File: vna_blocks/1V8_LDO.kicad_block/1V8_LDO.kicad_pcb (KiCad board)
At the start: 4 copper layers, 8 parts, among them U39 LT3041ADE-PBF

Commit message: hmc7044 design block
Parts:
- removed C347, C351, C353: 10u, Capacitor_SMD:C_0402_1005Metric
- removed C349: 4.7u, Capacitor_SMD:C_0603_1608Metric
- removed R190: 18k, Resistor_SMD:R_0402_1005Metric
- removed R193: 43k, Resistor_SMD:R_0402_1005Metric
- removed R194: 10k, Resistor_SMD:R_0402_1005Metric
- removed U39: LT3041ADE-PBF, VNA_fp:05-08-1708_ADI-L
- added C346: 10u, Capacitor_SMD:C_0402_1005Metric, B.Cu at (238.8, 96.0)
- added C348: 4.7u, Capacitor_SMD:C_0603_1608Metric, B.Cu at (241.2, 103.6)
- added C350: 10u, Capacitor_SMD:C_0402_1005Metric, B.Cu at (238.4, 101.4)
- added C352: 10u, Capacitor_SMD:C_0402_1005Metric, B.Cu at (238.4, 102.6)
- added R189: 18k, Resistor_SMD:R_0402_1005Metric, B.Cu at (241.0, 101.4)
- added R191: 43k, Resistor_SMD:R_0402_1005Metric, B.Cu at (242.8, 102.0)
- added R192: 10k, Resistor_SMD:R_0402_1005Metric, B.Cu at (244.4, 101.4)
- added U38: LT3041ADE-PBF, VNA_fp:05-08-1708_ADI-L, B.Cu at (240.4, 98.8)

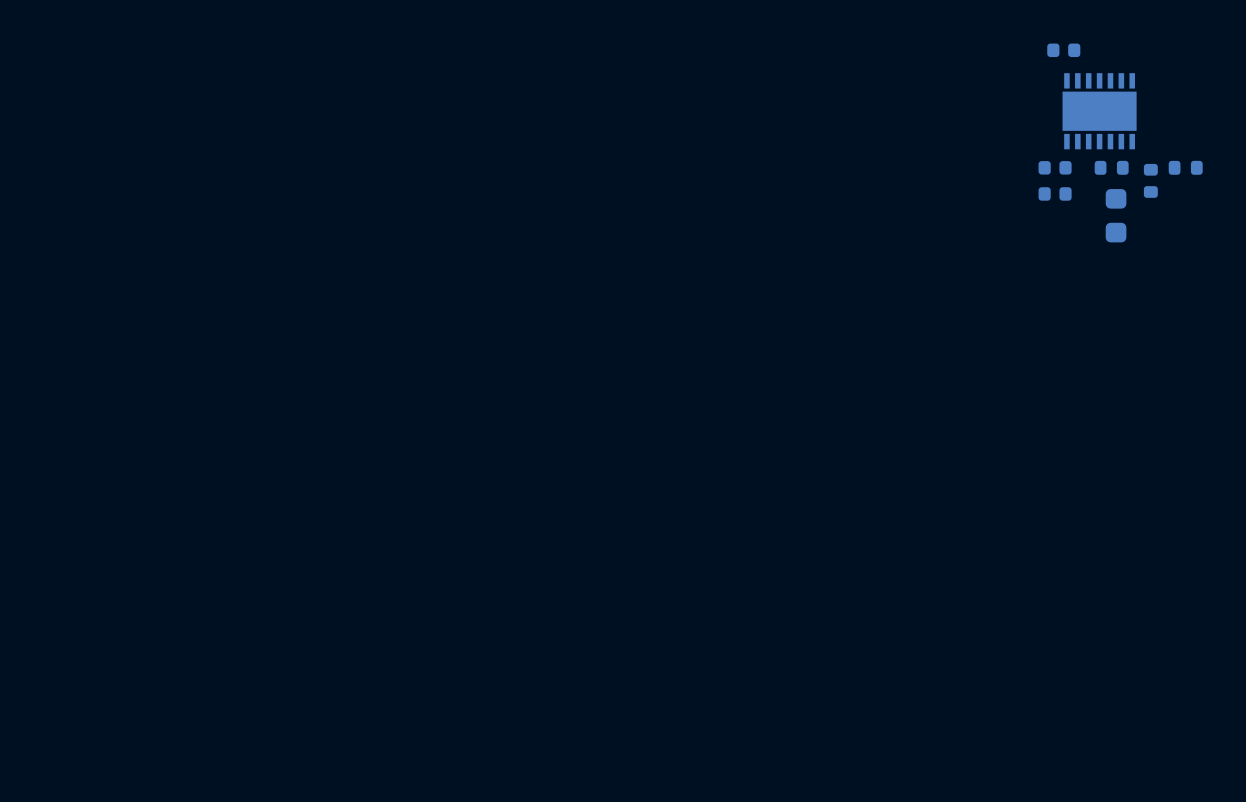
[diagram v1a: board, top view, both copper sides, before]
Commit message: fixed IC courtyard issues
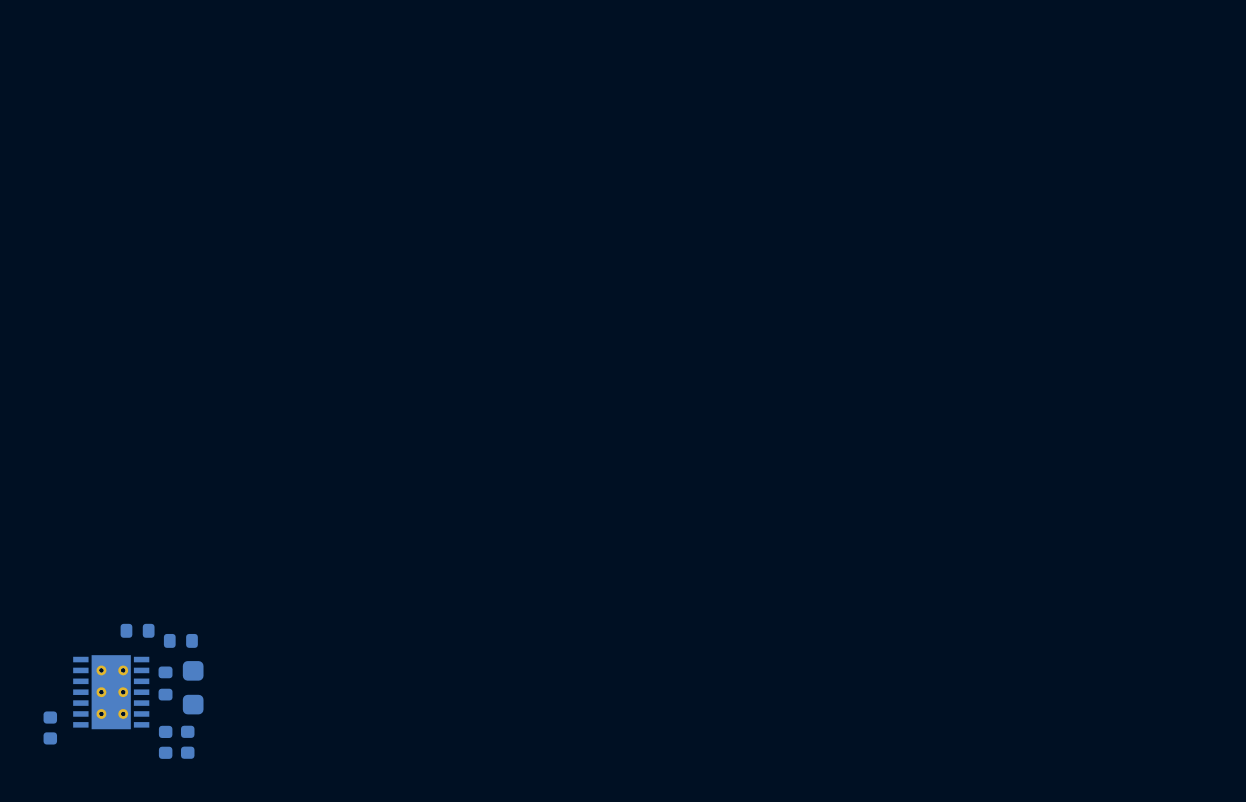
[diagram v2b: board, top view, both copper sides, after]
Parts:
- moved C346 56.0 mm to (192.2, 127.1), turned to 90 degrees
- moved U38 52.7 mm to (195.0, 125.5), turned to 0 degrees
- moved R192 52.6 mm to (196.2, 122.7), turned to 0 degrees
- moved R189 49.5 mm to (197.5, 125.1), turned to 90 degrees
- moved R191 49.3 mm to (198.2, 123.1), turned to 0 degrees
- moved C350 48.6 mm to (197.5, 127.8), turned to -90 degrees
- moved C348 47.6 mm to (198.8, 125.3)
- moved C352 47.1 mm to (198.5, 127.8), turned to -90 degrees
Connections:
- net /1V8A renamed /1V8ADC1
- net /Power/+3V8_in renamed /Power/3V8_int
- net /Power/1V8/PGFB_1V8A renamed /Power/1V8/PGFB_1V8ADC1
- net EN_DIG renamed /EN_DIG
- net PG_DIG renamed /PG_DIG
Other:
- copper layers 4 -> 8
